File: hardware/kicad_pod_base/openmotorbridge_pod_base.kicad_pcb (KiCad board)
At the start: 2 copper layers, 36 x 20 mm, 6 parts

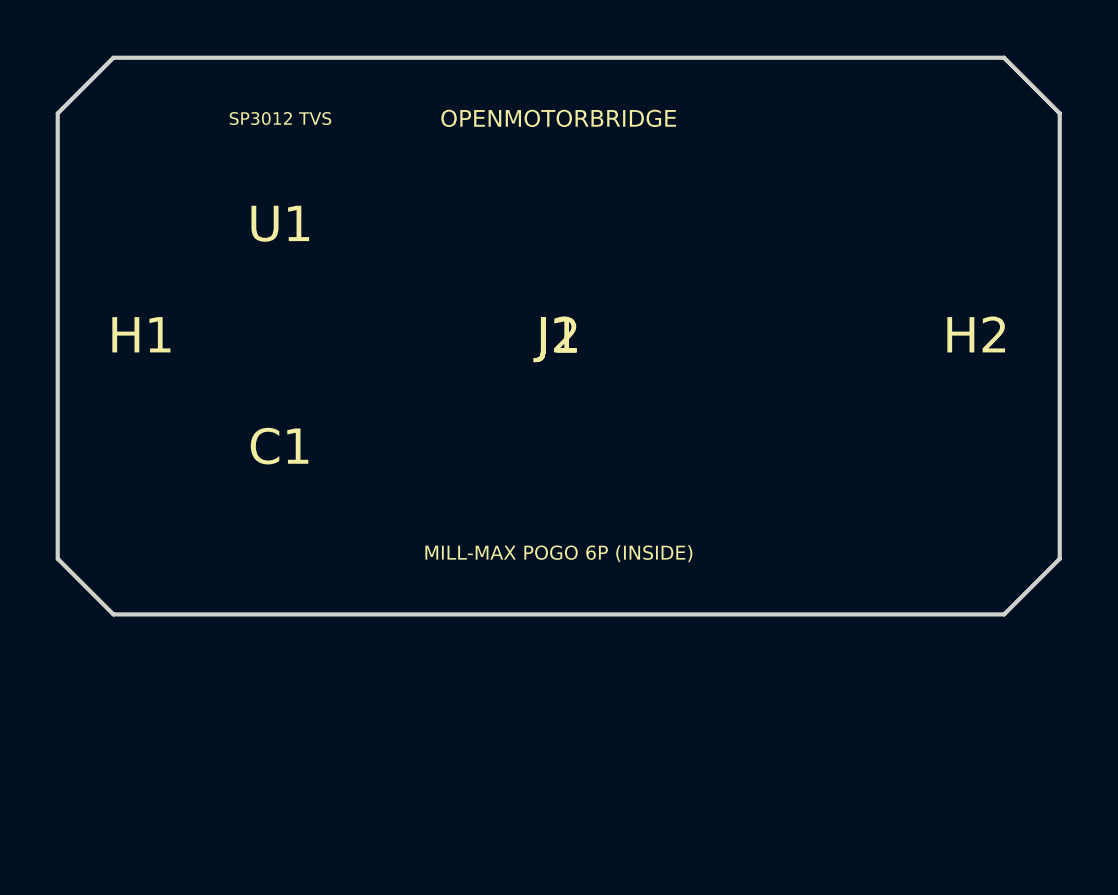
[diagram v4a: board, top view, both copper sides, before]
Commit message: hardware(cad/renders): update 3D board renders and mechanical CAD assembly for centric cartridge sled and horizontal mating
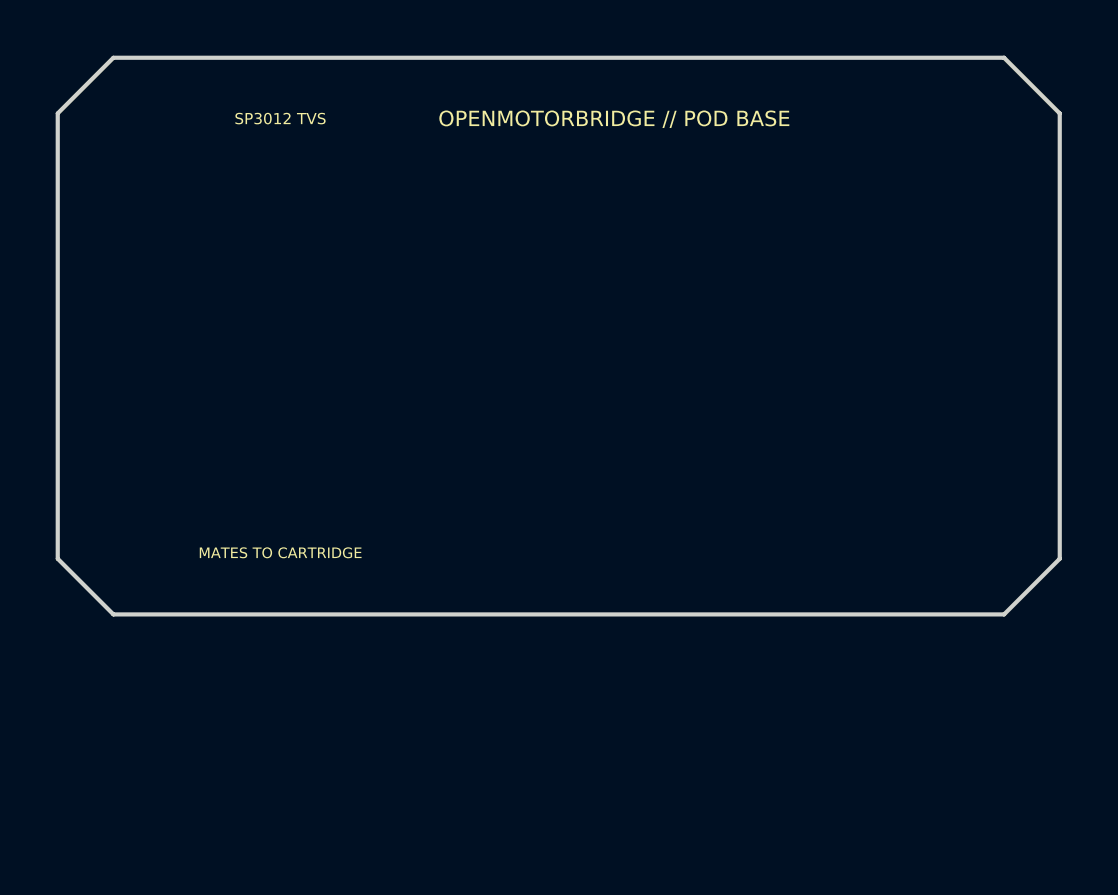
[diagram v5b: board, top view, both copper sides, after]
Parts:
- moved J1 6.35 mm to (118.0, 73.7)
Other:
- board text added: "MATES TO CARTRIDGE"
- board text added: "OPENMOTORBRIDGE // POD BASE"
- board text removed: "MILL-MAX POGO 6P (INSIDE)"
- board text removed: "OPENMOTORBRIDGE"
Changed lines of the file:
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@@
 	(footprint ""
 		(layer "F.Cu")
-		(at 118 80)
+		(at 108 84)
+		(property "Reference" "C1"
+			(at 0 0 0)
+			(layer "F.SilkS")
+			(hide yes)
+			(effects
+				(font
+					(size 1.27 1.27)
+				)
+			)
+		)
+		(property "Value" ""
+			(at 0 0 0)
+			(layer "F.Fab")
+			(effects
+				(font
+					(size 1.27 1.27)
+				)
+			)
+		)
+		(property "Datasheet" ""
+			(at 0 0 0)
+			(layer "F.Fab")
+			(hide yes)
+			(effects
+				(font
+					(size 1.27 1.27)
+				)
+			)
+		)
+		(property "Description" ""
+			(at 0 0 0)
+			(layer "F.Fab")
+			(hide yes)
+			(effects
+				(font
+					(size 1.27 1.27)
+				)
+			)
+		)
+		(duplicate_pad_numbers_are_jumpers no)
+		(embedded_fonts no)
+		(model "${KICAD10_3DMODEL_DIR}/Capacitor_SMD.3dshapes/C_0603_1608Metric.step"
+			(offset
+				(xyz 0 0 0)
+			)
+			(scale
+				(xyz 1 1 1)
+			)
+			(rotate
+				(xyz 0 0 0)
+			)
+		)
+	)
+	(footprint ""
+		(layer "F.Cu")
+		(at 118 73.65)
 		(property "Reference" "J1"
 			(at 0 0 0)
 			(layer "F.SilkS")
-			(effects
-				(font
-					(size 1.27 1.27)
-				)
-			)
-		)
-		(property "Value" ""
-			(at 0 0 0)
-			(layer "F.Fab")
-			(effects
-				(font
-					(size 1.27 1.27)
-				)
-			)
-		)
-		(property "Datasheet" ""
-			(at 0 0 0)
-			(layer "F.Fab")
-			(hide yes)
-			(effects
-				(font
-					(size 1.27 1.27)
-				)
-			)
-		)
-		(property "Description" ""
-			(at 0 0 0)
-			(layer "F.Fab")
-			(hide yes)
-			(effects
-				(font
-					(size 1.27 1.27)
-				)
-			)
-		)
-		(duplicate_pad_numbers_are_jumpers no)
-		(embedded_fonts no)
-		(model "${KICAD10_3DMODEL_DIR}/Connector_PinHeader_2.54mm.3dshapes/PinHeader_1x06_P2.54mm_Vertical.step"
+			(hide yes)
+			(effects
+				(font
+					(size 1.27 1.27)
+				)
+			)
+		)
+		(property "Value" ""
+			(at 0 0 0)
+			(layer "F.Fab")
+			(effects
+				(font
+					(size 1.27 1.27)
+				)
+			)
+		)
+		(property "Datasheet" ""
+			(at 0 0 0)
+			(layer "F.Fab")
+			(hide yes)
+			(effects
+				(font
+					(size 1.27 1.27)
+				)
+			)
+		)
+		(property "Description" ""
+			(at 0 0 0)
+			(layer "F.Fab")
+			(hide yes)
+			(effects
+				(font
+					(size 1.27 1.27)
+				)
+			)
+		)
+		(duplicate_pad_numbers_are_jumpers no)
+		(embedded_fonts no)
+		(model "${KICAD10_3DMODEL_DIR}/Connector_PinHeader_2.54mm.3dshapes/PinHeader_1x06_P2.54mm_Horizontal.step"
 			(offset
-				(xyz 0 6.35 0)
+				(xyz 0 0 0)
+			)
+			(scale
+				(xyz 1 1 1)
+			)
+			(rotate
+				(xyz 0 0 0)
+			)
+		)
+	)
+	(footprint ""
+		(layer "F.Cu")
+		(at 108 76)
+		(property "Reference" "U1"
+			(at 0 0 0)
+			(layer "F.SilkS")
+			(hide yes)
+			(effects
+				(font
+					(size 1.27 1.27)
+				)
+			)
+		)
+		(property "Value" ""
+			(at 0 0 0)
+			(layer "F.Fab")
+			(effects
+				(font
+					(size 1.27 1.27)
+				)
+			)
+		)
+		(property "Datasheet" ""
+			(at 0 0 0)
+			(layer "F.Fab")
+			(hide yes)
+			(effects
+				(font
+					(size 1.27 1.27)
+				)
+			)
+		)
+		(property "Description" ""
+			(at 0 0 0)
+			(layer "F.Fab")
+			(hide yes)
+			(effects
+				(font
+					(size 1.27 1.27)
+				)
+			)
+		)
+		(duplicate_pad_numbers_are_jumpers no)
+		(embedded_fonts no)
+		(model "${KICAD10_3DMODEL_DIR}/Package_DFN_QFN.3dshapes/DFN-14-1EP_3x3mm_P0.4mm_EP1.78x2.35mm.step"
+			(offset
+				(xyz 0 0 0)
 			)
 			(scale
@@
 			(at 0 0 0)
 			(layer "F.SilkS")
+			(hide yes)
 			(effects
 				(font
@@
 			(at 0 0 0)
 			(layer "F.SilkS")
-			(effects
-				(font
-					(size 1.27 1.27)
-				)
-			)
-		)
-		(property "Value" ""
-			(at 0 0 0)
-			(layer "F.Fab")
-			(effects
-				(font
-					(size 1.27 1.27)
-				)
-			)
-		)
-		(property "Datasheet" ""
-			(at 0 0 0)
-			(layer "F.Fab")
-			(hide yes)
-			(effects
-				(font
-					(size 1.27 1.27)
-				)
-			)
-		)
-		(property "Description" ""
-			(at 0 0 0)
-			(layer "F.Fab")
-			(hide yes)
-			(effects
-				(font
-					(size 1.27 1.27)
-				)
-			)
-		)
-		(duplicate_pad_numbers_are_jumpers no)
-		(embedded_fonts no)
-	)
-	(footprint ""
-		(layer "F.Cu")
-		(at 108 84)
-		(property "Reference" "C1"
-			(at 0 0 0)
-			(layer "F.SilkS")
-			(effects
-				(font
-					(size 1.27 1.27)
-				)
-			)
-		)
-		(property "Value" ""
-			(at 0 0 0)
-			(layer "F.Fab")
-			(effects
-				(font
-					(size 1.27 1.27)
-				)
-			)
-		)
-		(property "Datasheet" ""
-			(at 0 0 0)
-			(layer "F.Fab")
-			(hide yes)
-			(effects
-				(font
-					(size 1.27 1.27)
-				)
-			)
-		)
-		(property "Description" ""
-			(at 0 0 0)
-			(layer "F.Fab")
-			(hide yes)
-			(effects
-				(font
-					(size 1.27 1.27)
-				)
-			)
-		)
-		(duplicate_pad_numbers_are_jumpers no)
-		(embedded_fonts no)
-		(model "${KICAD10_3DMODEL_DIR}/Capacitor_SMD.3dshapes/C_0603_1608Metric.step"
-			(offset
-				(xyz 0 0 0)
-			)
-			(scale
-				(xyz 1 1 1)
-			)
-			(rotate
-				(xyz 0 0 0)
-			)
-		)
-	)
-	(footprint ""
-		(layer "F.Cu")
-		(at 108 76)
-		(property "Reference" "U1"
-			(at 0 0 0)
-			(layer "F.SilkS")
-			(effects
-				(font
-					(size 1.27 1.27)
-				)
-			)
-		)
-		(property "Value" ""
-			(at 0 0 0)
-			(layer "F.Fab")
-			(effects
-				(font
-					(size 1.27 1.27)
-				)
-			)
-		)
-		(property "Datasheet" ""
-			(at 0 0 0)
-			(layer "F.Fab")
-			(hide yes)
-			(effects
-				(font
-					(size 1.27 1.27)
-				)
-			)
-		)
-		(property "Description" ""
-			(at 0 0 0)
-			(layer "F.Fab")
-			(hide yes)
-			(effects
-				(font
-					(size 1.27 1.27)
-				)
-			)
-		)
-		(duplicate_pad_numbers_are_jumpers no)
-		(embedded_fonts no)
-		(model "${KICAD10_3DMODEL_DIR}/Package_DFN_QFN.3dshapes/DFN-14-1EP_3x3mm_P0.4mm_EP1.78x2.35mm.step"
-			(offset
-				(xyz 0 0 0)
-			)
-			(scale
-				(xyz 1 1 1)
-			)
-			(rotate
-				(xyz 0 0 0)
-			)
-		)
+			(hide yes)
+			(effects
+				(font
+					(size 1.27 1.27)
+				)
+			)
+		)
+		(property "Value" ""
+			(at 0 0 0)
+			(layer "F.Fab")
+			(effects
+				(font
+					(size 1.27 1.27)
+				)
+			)
+		)
+		(property "Datasheet" ""
+			(at 0 0 0)
+			(layer "F.Fab")
+			(hide yes)
+			(effects
+				(font
+					(size 1.27 1.27)
+				)
+			)
+		)
+		(property "Description" ""
+			(at 0 0 0)
+			(layer "F.Fab")
+			(hide yes)
+			(effects
+				(font
+					(size 1.27 1.27)
+				)
+			)
+		)
+		(duplicate_pad_numbers_are_jumpers no)
+		(embedded_fonts no)
 	)
 	(footprint ""
@@
 			(at 0 0 0)
 			(layer "F.SilkS")
+			(hide yes)
 			(effects
 				(font
@@
 			)
 			(scale
-				(xyz 1 1 1)
+				(xyz 393.700787 393.700787 393.700787)
 			)
 			(rotate
@@
 		)
 		(layer "Edge.Cuts")
+	)
+	(gr_text "MATES TO CARTRIDGE"
+		(at 108 87.8 0)
+		(layer "F.SilkS")
+		(effects
+			(font
+				(size 0.38 0.38)
+				(thickness 0.08)
+			)
+		)
 	)
 	(gr_text "SP3012 TVS"
@@
 		(effects
 			(font
-				(size 0.45 0.45)
-				(thickness 0.1)
-			)
-		)
-	)
-	(gr_text "MILL-MAX POGO 6P (INSIDE)"
-		(at 118 87.8 0)
+				(size 0.4 0.4)
+				(thickness 0.09)
+			)
+		)
+	)
+	(gr_text "OPENMOTORBRIDGE // POD BASE"
+		(at 120 72.2 0)
 		(layer "F.SilkS")
 		(effects
 			(font
-				(size 0.5 0.5)
-				(thickness 0.1)
-			)
-		)
-	)
-	(gr_text "OPENMOTORBRIDGE"
-		(at 118 72.2 0)
-		(layer "F.SilkS")
-		(effects
-			(font
-				(size 0.6 0.6)
-				(thickness 0.12)
-			)
-		)
+				(size 0.55 0.55)
+				(thickness 0.11)
+			)
+		)
